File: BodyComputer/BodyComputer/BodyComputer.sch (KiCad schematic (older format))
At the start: 1 part

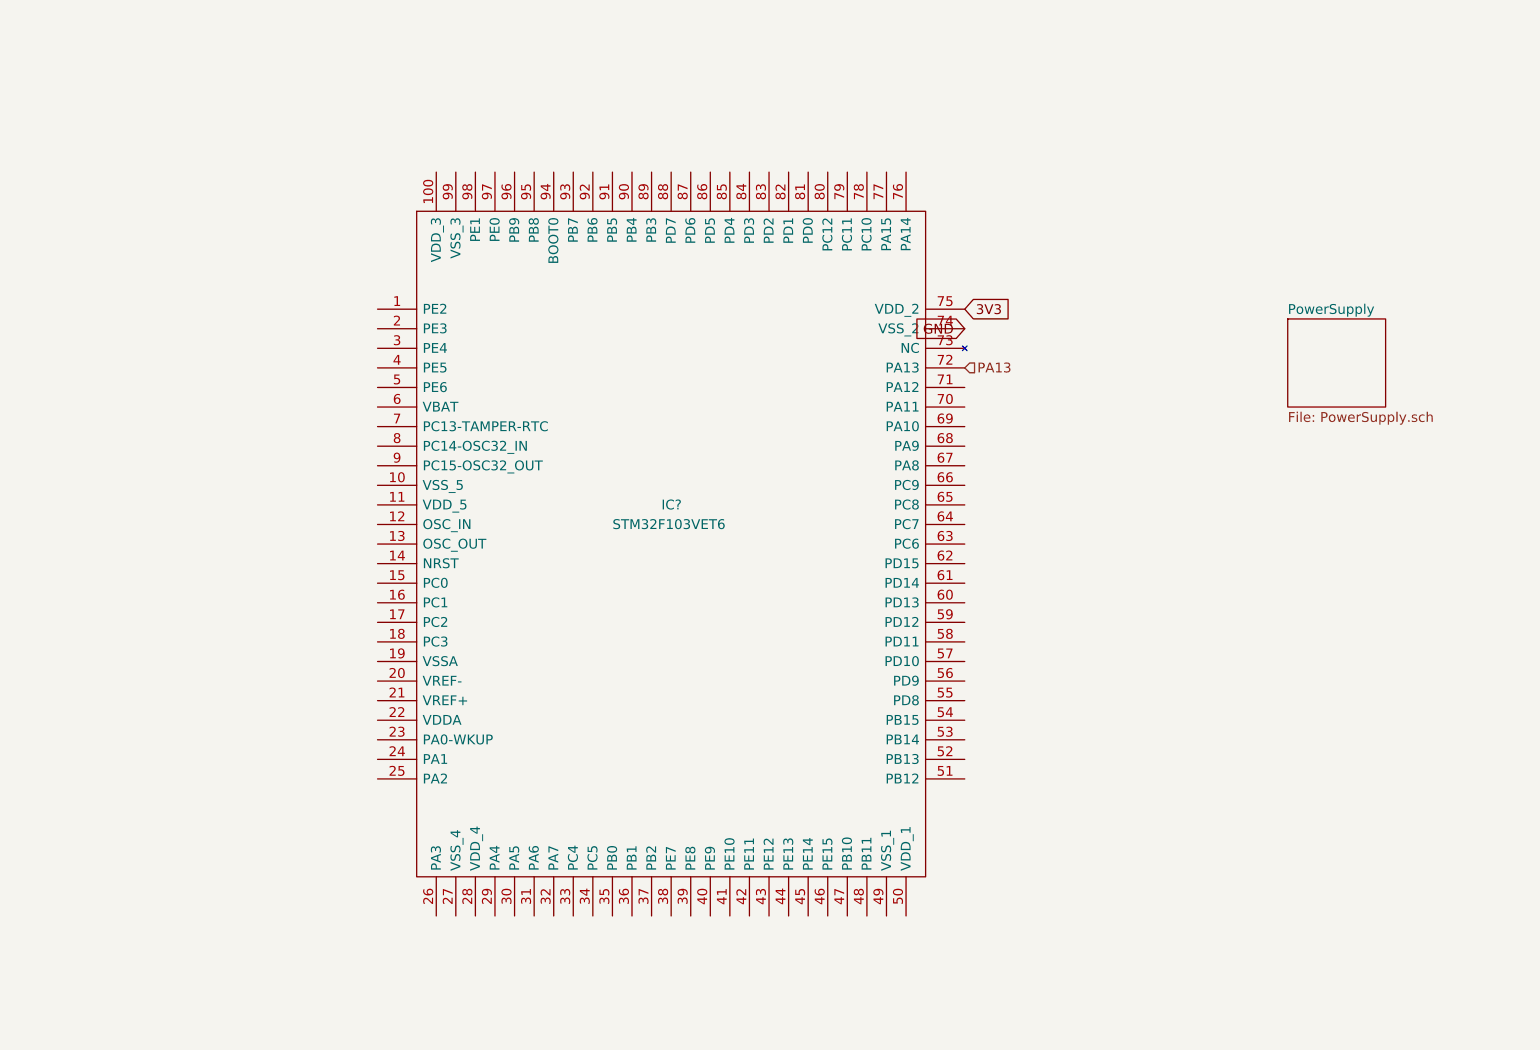
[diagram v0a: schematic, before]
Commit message: First version of the schematic
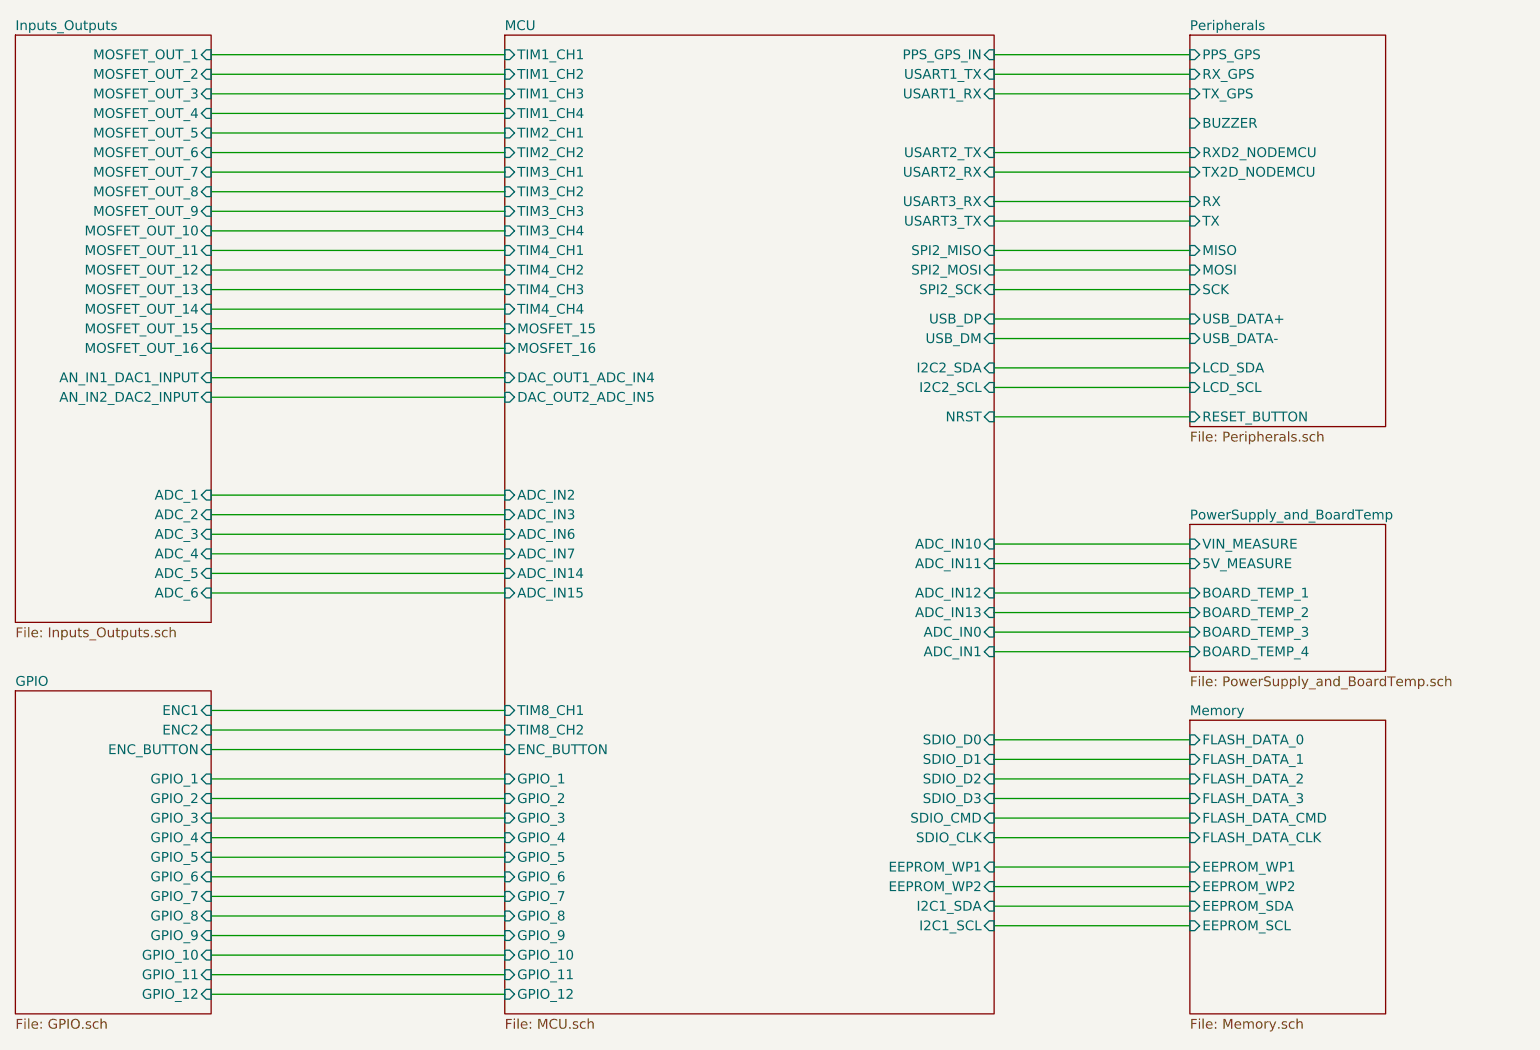
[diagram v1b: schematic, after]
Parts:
- removed IC?: STM32F103VET6, QFP50P1600X1600X160-100N, symbol SamacSys_Parts:STM32F103VET6

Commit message: Update due to moving to another computer. Updated Schematic, Print-outs, PCB in development
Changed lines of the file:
@@
 Sheet 1 7
 Title "Body Computer"
-Date "2020-03-09"
+Date "2020-03-19"
 Rev "1.0"
 Comp "Wojciech Grzeliński"
@@
 F4 "BOARD_TEMP_1" I L 8500 3850 50
 F5 "BOARD_TEMP_2" I L 8500 3950 50
-F6 "BOARD_TEMP_3" I L 8500 4050 50
-F7 "BOARD_TEMP_4" I L 8500 4150 50
 $EndSheet
 $Sheet
@@
 F18 "AN_IN1_DAC1_INPUT" I R 3500 2750 50
 F19 "AN_IN2_DAC2_INPUT" I R 3500 2850 50
-F20 "ADC_1" I R 3500 3350 50
-F21 "ADC_2" I R 3500 3450 50
-F22 "ADC_3" I R 3500 3550 50
-F23 "ADC_4" I R 3500 3650 50
-F24 "ADC_5" I R 3500 3750 50
-F25 "ADC_6" I R 3500 3850 50
+F20 "ADC_1" I R 3500 3150 50
+F21 "ADC_2" I R 3500 3250 50
+F22 "ADC_3" I R 3500 3350 50
+F23 "ADC_4" I R 3500 3450 50
+F24 "ADC_5" I R 3500 3550 50
+F25 "ADC_6" I R 3500 3650 50
+F26 "ADC_7" I R 3500 3750 50
+F27 "ADC_8" I R 3500 3850 50
 $EndSheet
 Wire Wire Line
@@
 F23 "ADC_IN12" I R 7500 3850 50
 F24 "ADC_IN13" I R 7500 3950 50
-F25 "ADC_IN0" I R 7500 4050 50
-F26 "ADC_IN1" I R 7500 4150 50
-F27 "ADC_IN2" I L 5000 3350 50
-F28 "ADC_IN3" I L 5000 3450 50
+F25 "ADC_IN0" I L 5000 3750 50
+F26 "ADC_IN1" I L 5000 3850 50
+F27 "ADC_IN2" I L 5000 3150 50
+F28 "ADC_IN3" I L 5000 3250 50
 F29 "DAC_OUT1_ADC_IN4" I L 5000 2750 50
 F30 "DAC_OUT2_ADC_IN5" I L 5000 2850 50
-F31 "ADC_IN6" I L 5000 3550 50
-F32 "ADC_IN7" I L 5000 3650 50
-F33 "ADC_IN14" I L 5000 3750 50
-F34 "ADC_IN15" I L 5000 3850 50
+F31 "ADC_IN6" I L 5000 3350 50
+F32 "ADC_IN7" I L 5000 3450 50
+F33 "ADC_IN14" I L 5000 3550 50
+F34 "ADC_IN15" I L 5000 3650 50
 F35 "USART1_RX" I R 7500 1300 50
 F36 "USART1_TX" I R 7500 1200 50
@@
 	7500 4600 8500 4600
 Wire Wire Line
-	8500 4150 7500 4150
-Wire Wire Line
-	7500 4050 8500 4050
-Wire Wire Line
 	8500 3950 7500 3950
 Wire Wire Line
@@
 Wire Wire Line
 	3500 5900 5000 5900
+Wire Wire Line
+	3500 3150 5000 3150
+Wire Wire Line
+	5000 3250 3500 3250
 $EndSCHEMATC

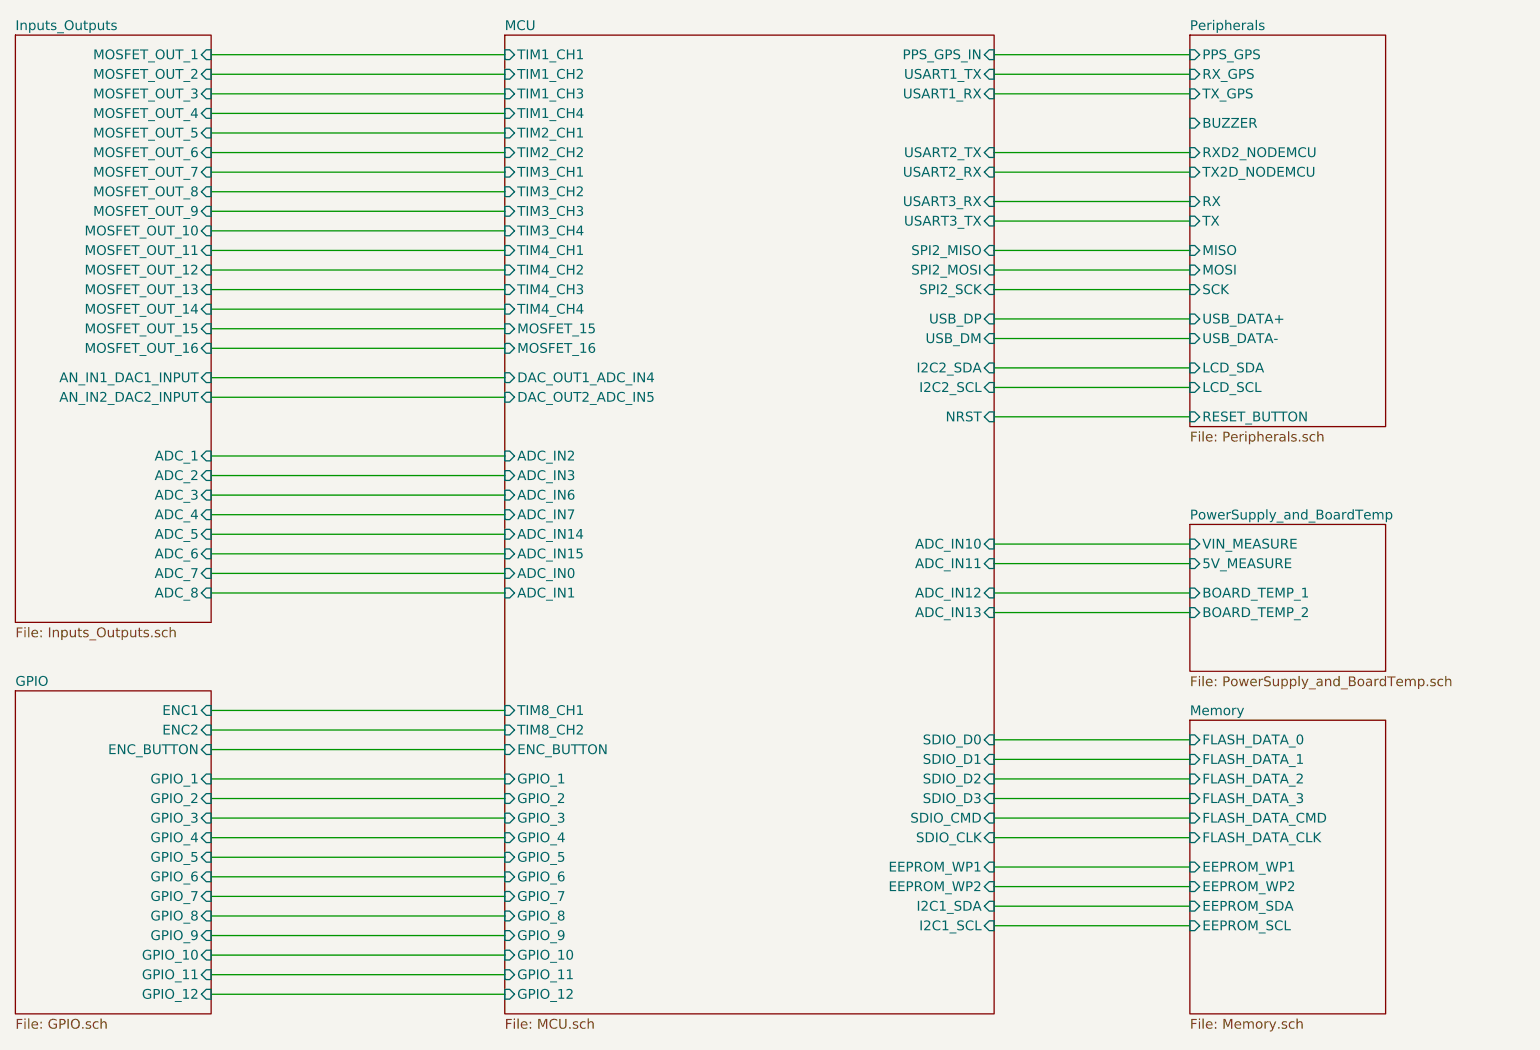
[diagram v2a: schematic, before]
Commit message: Updated schematic (DC/DC), 2-layer PCB
Updated schematic in multiple places, added elements, exchanged 3V3 stabilizer for a DC/DC converter. Nearly finished 2-layer PCB layout.
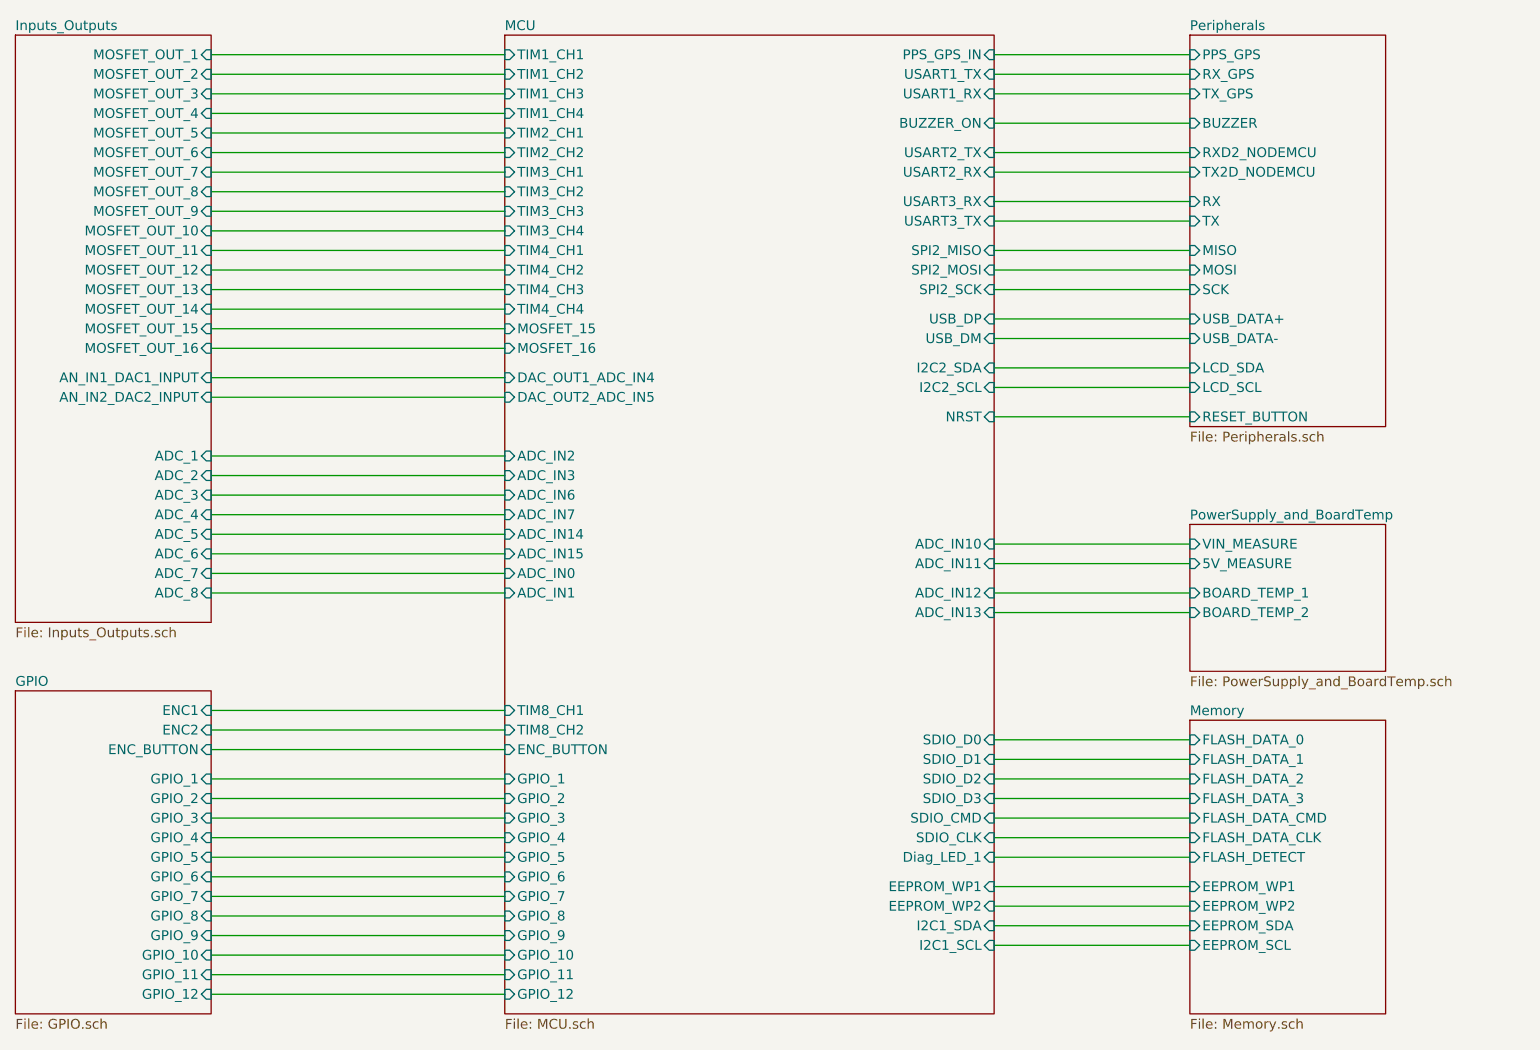
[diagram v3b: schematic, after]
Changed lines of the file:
@@
 Sheet 1 7
 Title "Body Computer"
-Date "2020-03-19"
+Date "2020-04-01"
 Rev "1.0"
 Comp "Wojciech Grzeliński"
@@
 F6 "FLASH_DATA_CMD" I L 8500 5000 50
 F7 "FLASH_DATA_1" I L 8500 4700 50
-F8 "EEPROM_SCL" I L 8500 5550 50
-F9 "EEPROM_SDA" I L 8500 5450 50
-F10 "EEPROM_WP1" I L 8500 5250 50
-F11 "EEPROM_WP2" I L 8500 5350 50
+F8 "EEPROM_SCL" I L 8500 5650 50
+F9 "EEPROM_SDA" I L 8500 5550 50
+F10 "EEPROM_WP1" I L 8500 5350 50
+F11 "EEPROM_WP2" I L 8500 5450 50
+F12 "FLASH_DETECT" I L 8500 5200 50
 $EndSheet
 $Sheet
@@
 F4 "SDIO_CLK" I R 7500 5100 50
 F5 "SDIO_CMD" I R 7500 5000 50
-F6 "I2C1_SDA" I R 7500 5450 50
-F7 "I2C1_SCL" I R 7500 5550 50
+F6 "I2C1_SDA" I R 7500 5550 50
+F7 "I2C1_SCL" I R 7500 5650 50
 F8 "I2C2_SDA" I R 7500 2700 50
 F9 "I2C2_SCL" I R 7500 2800 50
@@
 F56 "MOSFET_15" I L 5000 2500 50
 F57 "ENC_BUTTON" I L 5000 4650 50
-F58 "EEPROM_WP1" I R 7500 5250 50
-F59 "EEPROM_WP2" I R 7500 5350 50
+F58 "EEPROM_WP1" I R 7500 5350 50
+F59 "EEPROM_WP2" I R 7500 5450 50
 F60 "GPIO_1" I L 5000 4800 50
 F61 "GPIO_2" I L 5000 4900 50
@@
 F70 "GPIO_11" I L 5000 5800 50
 F71 "GPIO_12" I L 5000 5900 50
+F72 "Diag_LED_1" I R 7500 5200 50
+F73 "BUZZER_ON" I R 7500 1450 50
 $EndSheet
 Wire Wire Line
@@
 	5000 2850 3500 2850
 Wire Wire Line
-	8500 5550 7500 5550
-Wire Wire Line
-	7500 5450 8500 5450
-Wire Wire Line
-	8500 5350 7500 5350
-Wire Wire Line
-	7500 5250 8500 5250
+	8500 5650 7500 5650
+Wire Wire Line
+	7500 5550 8500 5550
+Wire Wire Line
+	8500 5450 7500 5450
+Wire Wire Line
+	7500 5350 8500 5350
 Wire Wire Line
 	8500 5100 7500 5100
@@
 Wire Wire Line
 	5000 3250 3500 3250
+Wire Wire Line
+	8500 5200 7500 5200
+Wire Wire Line
+	8500 1450 7500 1450
 $EndSCHEMATC
